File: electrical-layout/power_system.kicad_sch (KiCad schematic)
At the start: 21 parts, among them K1 DNCLEV100, K2 JD2912-48V, K3 JD2912-48V, K4 DNCLEV100, K5 DNCLEV100, K6 DNCLEV100, SW1 SW_Push, U1 Outdrive 5.0, U2 Protium-2500, U3 Protium-2500, U4 BBMP_S

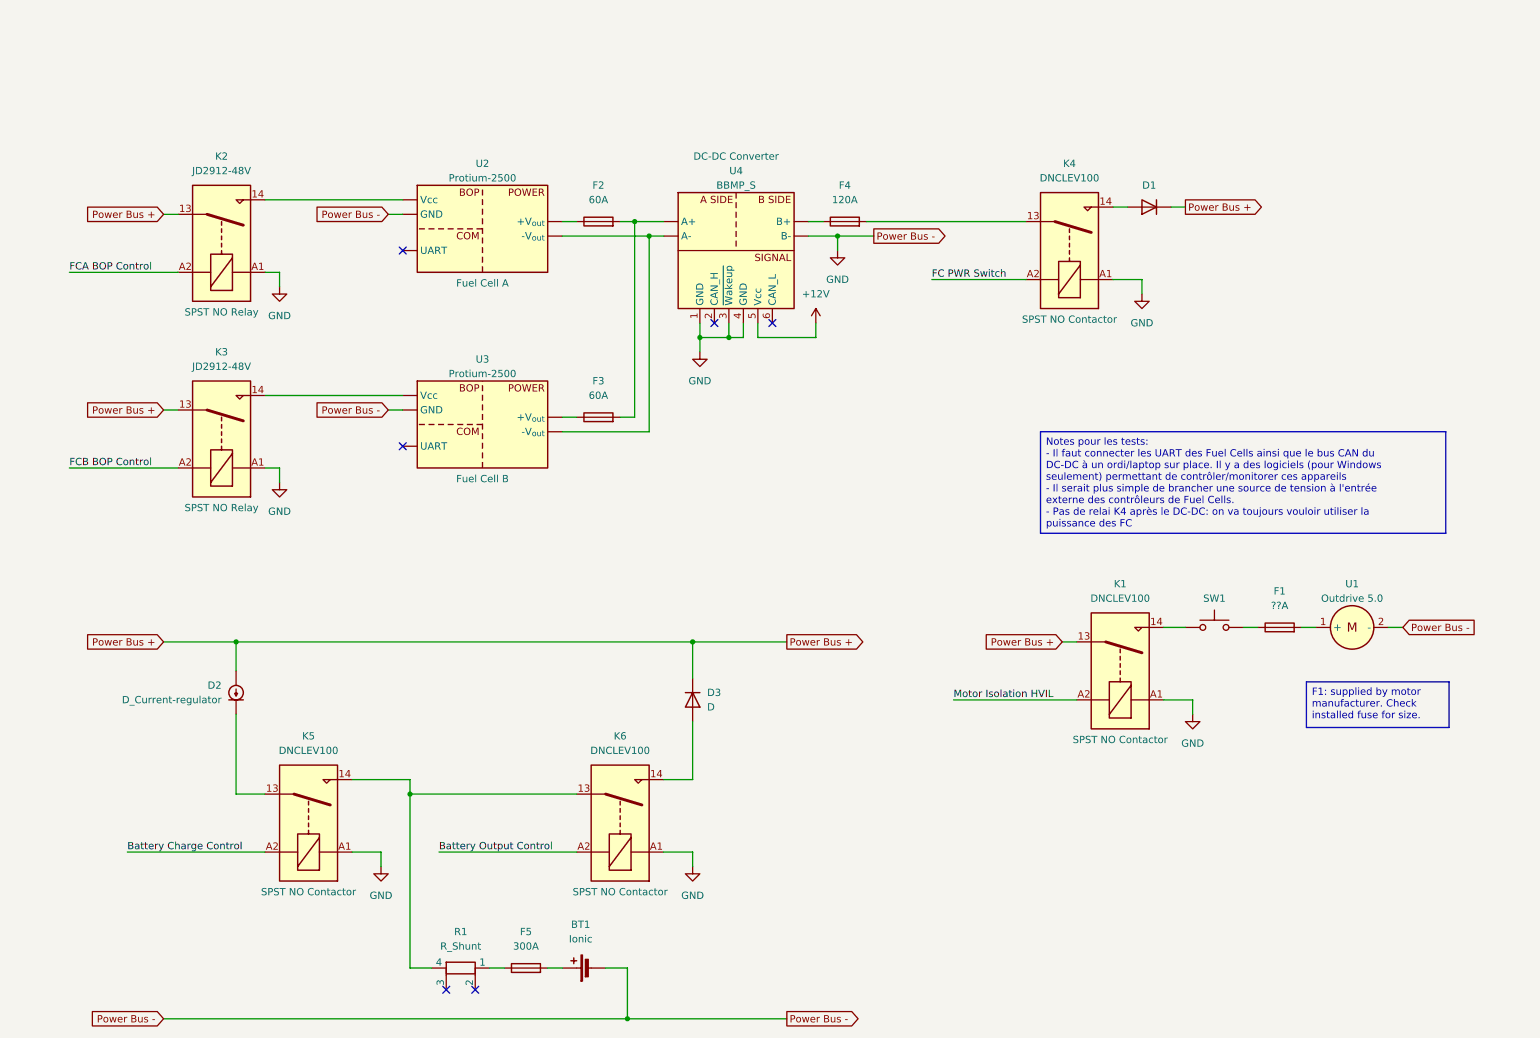
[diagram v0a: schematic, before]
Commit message: power-system: add DC-DC charger and temp. switches
This includes changes recommended to us during summer of 2025. Temporary
switch symbols have been used to indicate where to expect them, while
their internal circuit is not yet know and implemented. These will most
likely be replaced by some power transistors in the future.

A few control signals were added and are not yet connected to a control
board, but these shall be implemented on the power control PCB.
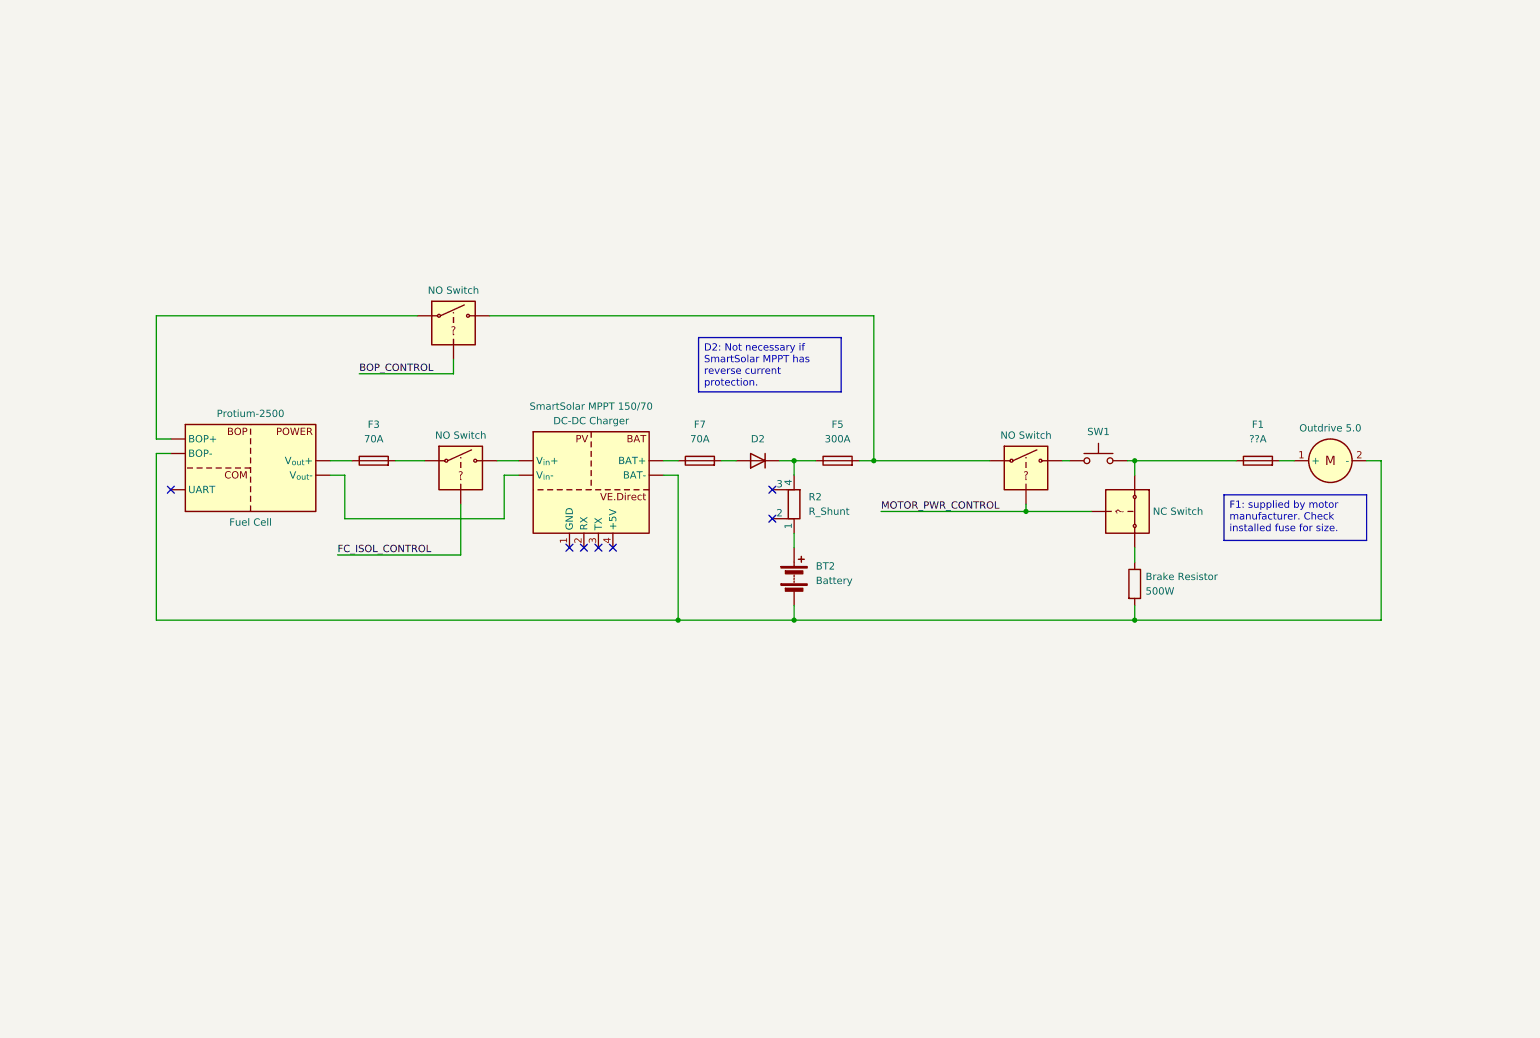
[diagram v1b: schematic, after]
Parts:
- removed BT1: Ionic, symbol Device:Battery_Cell
- removed D1, D3: D, symbol Device:D
- removed D2: D_Current-regulator, symbol Device:D_Current-regulator
- removed F2: 60A, symbol Device:Fuse
- removed F4: 120A, symbol Device:Fuse
- removed K1, K4, K5, K6: DNCLEV100, symbol Relay:Relay_SPST-NO
- removed K2, K3: JD2912-48V, symbol Relay:Relay_SPST-NO
- removed R1: R_Shunt, symbol Device:R_Shunt
- removed U2: Protium-2500, symbol Exocet:Protium-2500
- removed U4: BBMP_S, symbol Exocet:BBMP_S
- added BT2: Battery, symbol Device:Battery
- added D2: D, symbol Device:D
- added F7: 70A, symbol Device:Fuse
- added R1: 500W, symbol Device:R
- added R2: R_Shunt, symbol Device:R_Shunt
- added U15: SmartSolar MPPT 150/70, symbol Exocet:Victron_MPPT_150/70
- added U16, U2, U4: NO Switch, symbol Exocet:VC_Switch_NO
- added U17: NC Switch, symbol Exocet:VC_Switch_NC
- F3: value 60A -> 70A
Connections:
- net at F3.2: now also U16.
- net at F5.1: now also D2.1 (K), R2.4
- net at F5.2: now also U2., U4.
- net at SW1.1: now also U4.
- net at F1.1, SW1.2: now also U17.
- net GND: no longer names the net of U1.2 (-), U3. (V_{out}-)
- net GND: now also BT2.2 (-), R1.2, U15. (BAT-)
- new net: R1.1, U17.
- new net: U2., U3. (V_{out}-)
- new net: D2.2 (A), F7.2
- new net: F7.1, U15. (BAT-)
- new net: U15. (BAT-), U16.
- new net: U15. (BAT-), U3. (V_{out}-)
- new net: BT2.1 (+), R2.1
- new net BOP_CONTROL: U2.
- new net FC_ISOL_CONTROL: U16.
- new net MOTOR_PWR_CONTROL: U17., U4.
- now unconnected: U3. (-V_{out})
- no-connect marks 6 -> 7
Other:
- moved on the sheet: F1, SW1

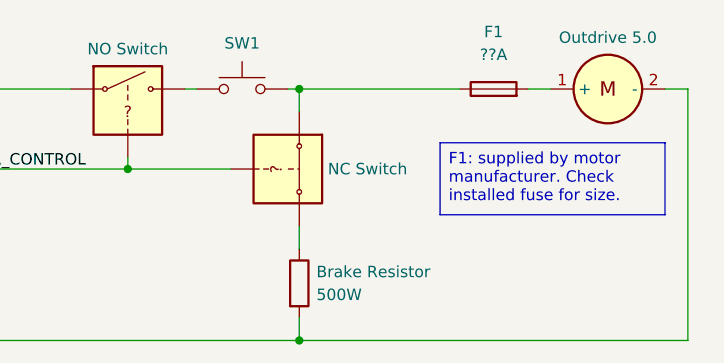
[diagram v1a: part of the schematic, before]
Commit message: layout-2025: update braking resistor value
Based on document from:
https://github.com/Exocet-Polytechnique/exo-electrical/issues/10
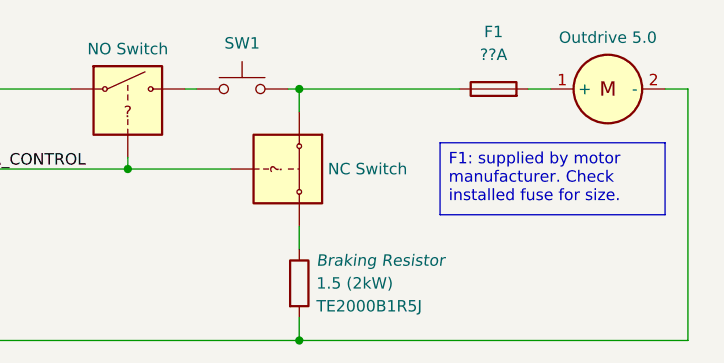
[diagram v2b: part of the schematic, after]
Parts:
- R1: value 500W -> 1.5 (2kW); Part (none) -> TE2000B1R5J
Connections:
- net at U3. (V_{out}-): no longer U2.
- net at U15. (BAT-): now also U3. (V_{out}-); no longer U16.
- new net: F5.2, U2., U4.
- new net: U2., U3. (V_{out}-)
- new net: U15. (BAT-), U16.
- now unconnected: U3. (V_{out}-)
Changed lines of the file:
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@@
 			)
 		)
-		(property "Value" "500W"
-			(at 211.455 114.3 0)
+		(property "Value" "1.5 (2kW)"
+			(at 211.455 113.03 0)
 			(effects
 				(font
@@
 			)
 		)
-		(property "Datasheet" "~"
+		(property "Datasheet" "https://www.te.com/en/product-1879456-3.html"
 			(at 209.55 113.03 0)
 			(effects
@@
 			)
 		)
-		(property "Description" "Brake Resistor"
-			(at 211.455 111.76 0)
+		(property "Description" "Braking Resistor"
+			(at 211.455 110.49 0)
 			(effects
 				(font
+					(size 1.27 1.27)
+					(italic yes)
+				)
+				(justify left)
+			)
+		)
+		(property "Part" "TE2000B1R5J"
+			(at 211.455 115.57 0)
+			(effects
+				(font

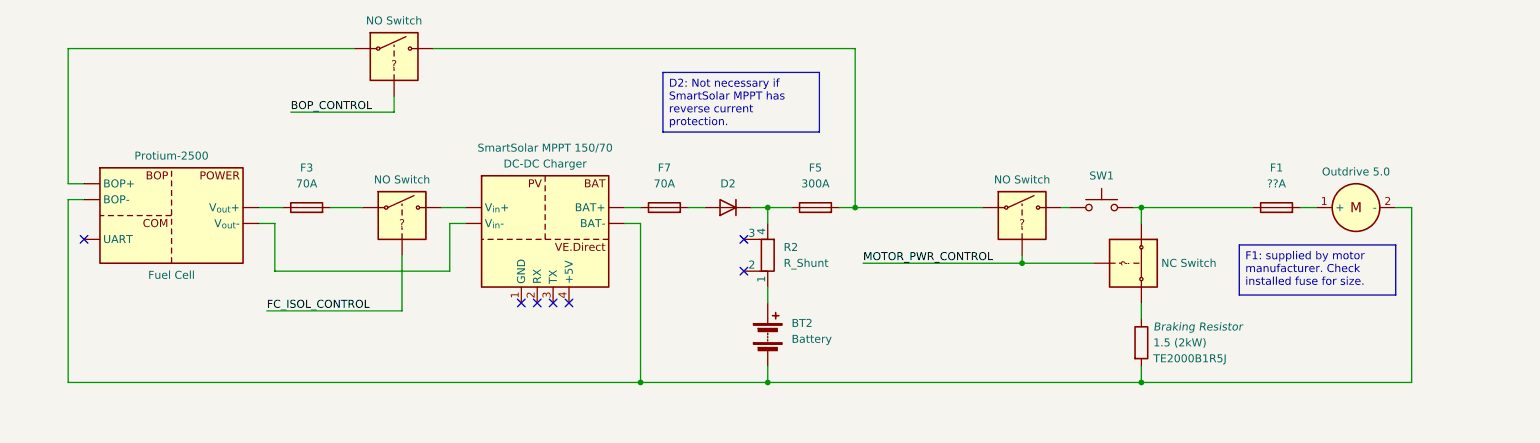
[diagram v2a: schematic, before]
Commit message: layout-2025: update some power symbols
New symbol for the charge controller now has two outputs: one for the
battery and one for the load. Also, its value was replaced with "TBD"
since we haven't decided on the actual model that will be used.

Some wires were replaced with power symbols to simplify the schematic.

A symbol was created for the cooling system and it was added to the
control box page. Since little is known about this system at the
moment, it is only represented by its power inputs. This power will
come from the main energy sources (fuel cells + auxiliary battery).

Information was added about the auxiliary battery model and capacity.
Many power symbols' fields were also uniformized to separate value,
part number, description and manufacturer.
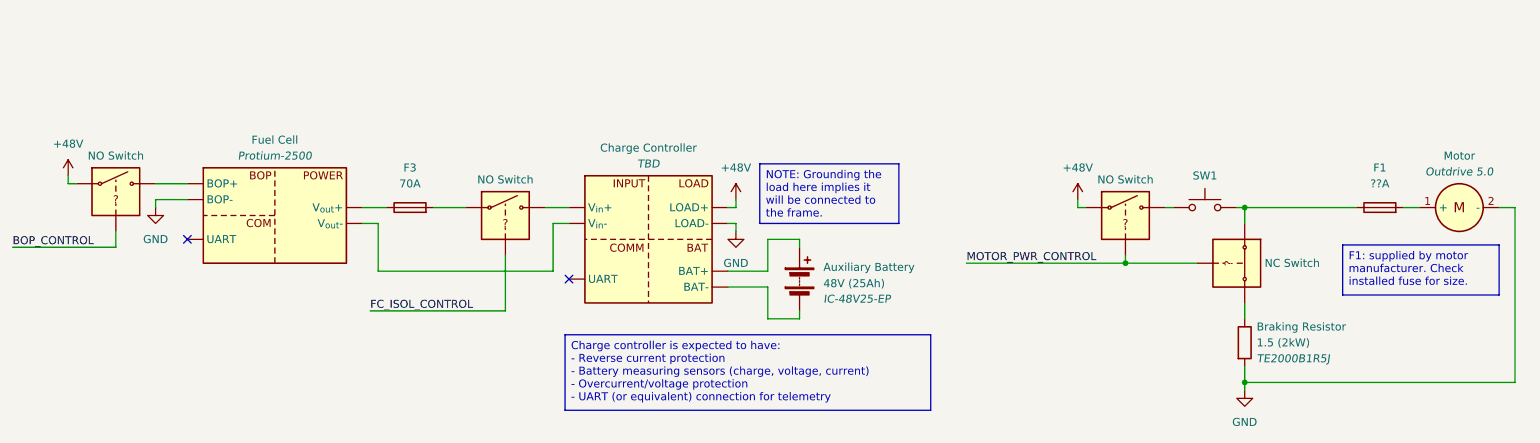
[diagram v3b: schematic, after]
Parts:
- removed D2: D, symbol Device:D
- removed F5: 300A, symbol Device:Fuse
- removed F7: 70A, symbol Device:Fuse
- removed R2: R_Shunt, symbol Device:R_Shunt
- removed U15: SmartSolar MPPT 150/70, symbol Exocet:Victron_MPPT_150/70
- added U19: ~, symbol Exocet:Charge_Controller
- BT2: value Battery -> 48V (25Ah); Manufacturer (none) -> Ionic; Part (none) -> IC-48V25-EP
- R1: Manufacturer (none) -> TE Connectivity
- U1: value Outdrive 5.0 -> ~; Manufacturer (none) -> Rim Drive Technology; Part (none) -> Outdrive 5.0
- U3: value Protium-2500 -> ~; Manufacturer (none) -> Spectronik; Part (none) -> Protium-2500
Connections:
- net GND: now reaches R1.2, U1.2 (-), U3. (V_{out}-)
- net GND: now also U19. (BAT-); no longer BT2.2 (-)
- net at BT2.1 (+): now also U19. (BAT-)
- new net: U2., U3. (V_{out}-)
- new net: U16., U19. (BAT-)
- new net: BT2.2 (-), U19. (BAT-)
- new net: U19. (BAT-), U3. (V_{out}-)
- new net +48V: U19. (BAT-), U2., U4.
- no-connect marks 7 -> 2
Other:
- moved on the sheet: F1, F3, SW1

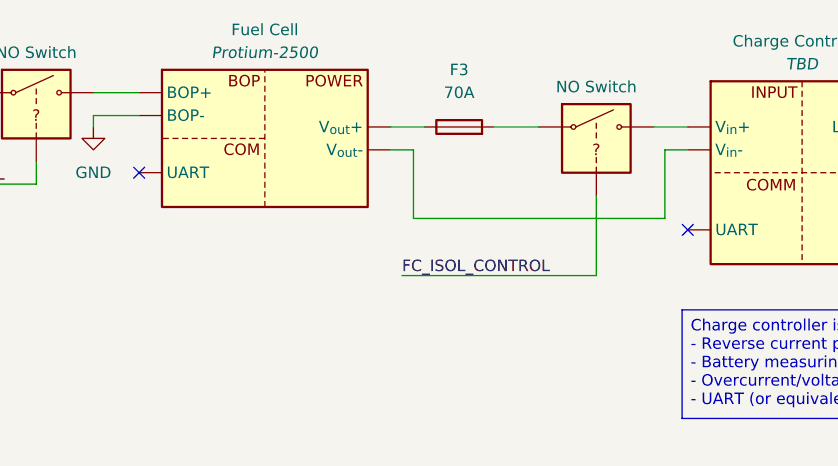
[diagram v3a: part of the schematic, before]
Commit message: layout-2025: add notes about fuel cell(s)
We might have more than one fuel cell in a series configuration
if their individual outputs are determined too low after testing.

Also, their output will need to be isolated from the frame because
it is over 60V. The isolation circuit will be added in a future
commit.
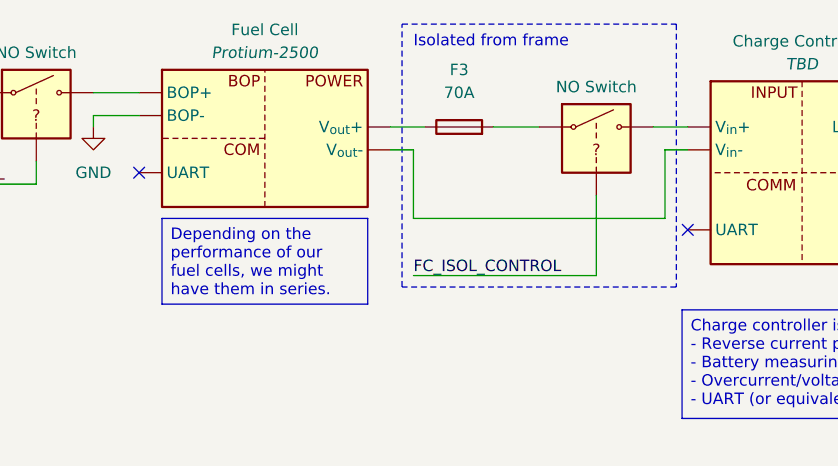
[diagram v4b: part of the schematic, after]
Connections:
- new net: U2., U3. (V_{out}-)
- new net: U16., U19. (BAT-)
- new net: U19. (BAT-), U3. (V_{out}-)
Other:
- note added: "Isolated from frame"
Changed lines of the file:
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@@
 		(rev "0.3.0")
+	)
+	(rectangle
+		(start 86.36 80.01)
+		(end 116.84 109.22)
+		(stroke
+			(width 0)
+			(type dash)
+		)
+		(fill
+			(type none)
+		)
+	)
+	(text "Isolated from frame"
+		(exclude_from_sim no)
+		(at 87.63 81.28 0)
+		(effects
+			(font
+				(size 1.27 1.27)
+			)
+			(justify left top)
+		)
 	)
 	(text_box "Charge controller is expected to have:\n- Reverse current protection\n- Battery measuring sensors (charge, voltage, current)\n- Overcurrent/voltage protection\n- UART (or equivalent) connection for telemetry"
@@
 		(at 117.475 111.76 0)
 		(size 58.42 12.065)
+		(margins 0.9525 0.9525 0.9525 0.9525)
+		(stroke
+			(width 0)
+			(type solid)
+		)
+		(fill
+			(type none)
+		)
+		(effects
+			(font
+				(size 1.27 1.27)
+			)
+			(justify left top)
+		)
+	)
+	(text_box "Depending on the performance of our fuel cells, we might have them in series."
+		(exclude_from_sim no)
+		(at 59.69 101.6 0)
+		(size 22.86 9.525)
 		(margins 0.9525 0.9525 0.9525 0.9525)
 		(stroke
@@
 	(wire
 		(pts
-			(xy 107.95 107.95) (xy 86.36 107.95)
+			(xy 107.95 107.95) (xy 87.63 107.95)
 		)
 		(stroke
@@
 	)
 	(label "FC_ISOL_CONTROL"
-		(at 86.36 107.95 0)
+		(at 87.63 107.95 0)
 		(effects
 			(font
